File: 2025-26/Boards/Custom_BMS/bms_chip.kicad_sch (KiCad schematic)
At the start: 56 parts, among them J7 Conn_01x06_Pin, J8 15246140, Q1 ZXTN4004KTC, U1 BQ79616PAPRQ1

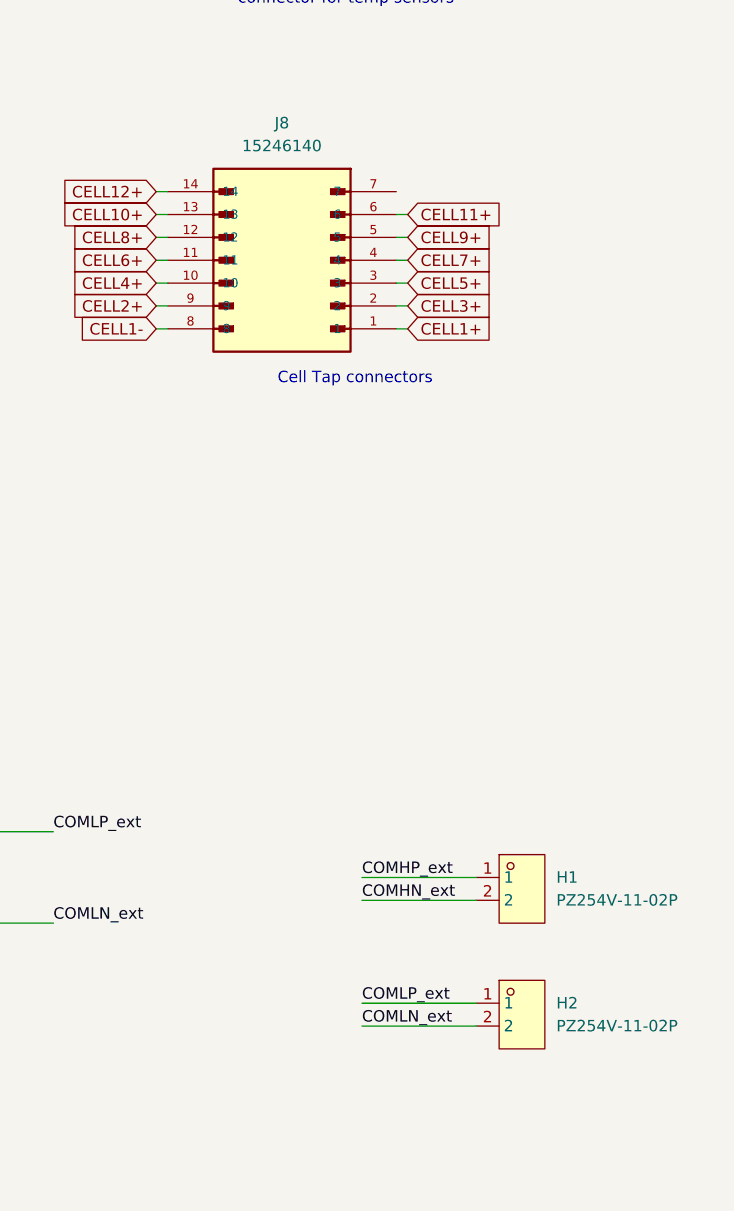
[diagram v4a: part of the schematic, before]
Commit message: fixed some connectors
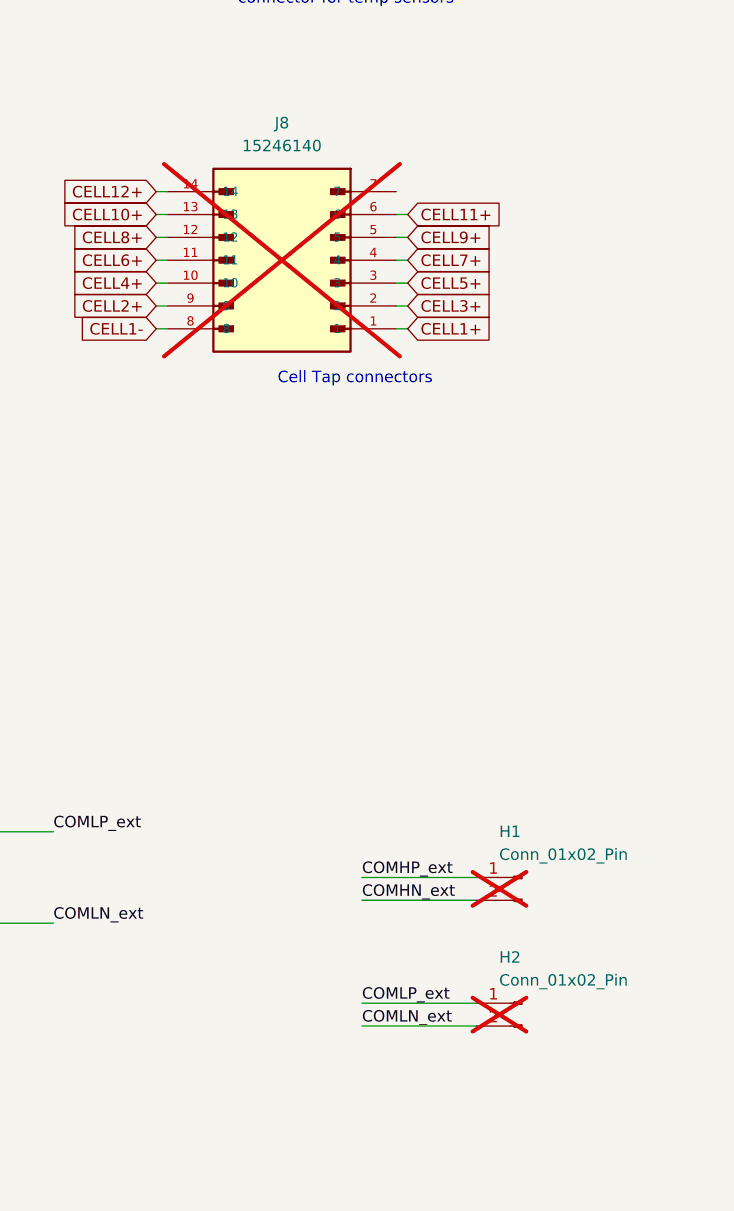
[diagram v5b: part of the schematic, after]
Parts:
- removed H1, H2: PZ254V-11-02P, easyeda2kicad:HDR-TH_2P-P2.54-V-M, symbol easyeda2kicad:PZ254V-11-02P
- added H1, H2: Conn_01x02_Pin, Connector_PinHeader_2.00mm:PinHeader_1x02_P2.00mm_Vertical, symbol Connector:Conn_01x02_Pin
- J8: now not fitted; now left out of the parts list
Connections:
- net COMHN_ext: now also H1.2 (Pin_2)
- net COMHP_ext: now also H1.1 (Pin_1)
- net COMLN_ext: now also H2.2 (Pin_2)
- net COMLP_ext: now also H2.1 (Pin_1)
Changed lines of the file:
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@@
 	)
 	(symbol
+		(lib_id "Connector:Conn_01x02_Pin")
+		(at 377.19 224.79 0)
+		(mirror y)
+		(unit 1)
+		(exclude_from_sim no)
+		(in_bom no)
+		(on_board yes)
+		(dnp yes)
+		(property "Reference" "H2"
+			(at 374.65 219.71 0)
+			(effects
+				(font
+					(size 1.27 1.27)
+				)
+				(justify right)
+			)
+		)
+		(property "Value" "Conn_01x02_Pin"
+			(at 374.65 222.25 0)
+			(effects
+				(font
+					(size 1.27 1.27)
+				)
+				(justify right)
+			)
+		)
+		(property "Footprint" "Connector_PinHeader_2.00mm:PinHeader_1x02_P2.00mm_Vertical"
+			(at 377.19 224.79 0)
+			(effects
+				(font
+					(size 1.27 1.27)
+				)
+				(hide yes)
+			)
+		)
+		(property "Datasheet" "~"
+			(at 377.19 224.79 0)
+			(effects
+				(font
+					(size 1.27 1.27)
+				)
+				(hide yes)
+			)
+		)
+		(property "Description" "Generic connector, single row, 01x02, script generated"
+			(at 377.19 224.79 0)
+			(effects
+				(font
+					(size 1.27 1.27)
+				)
+				(hide yes)
+			)
+		)
+		(pin "1"
+		)
+		(pin "2"
+		)
+		(instances
+			(project "Custom_BMS"
+				(path "/570d6d9c-ebf5-4f83-96f6-d3309a3e637d/730c9124-1e05-4e73-95cf-1be5bb1149a5"
+					(reference "H2")
+					(unit 1)
+				)
+			)
+		)
+	)
+	(symbol
 		(lib_id "PCM_JLCPCB-Resistors:0603,10kΩ")
 		(at 295.91 95.25 90)
@@
 	)
 	(symbol
+		(lib_id "Connector:Conn_01x02_Pin")
+		(at 377.19 210.82 0)
+		(mirror y)
+		(unit 1)
+		(exclude_from_sim no)
+		(in_bom no)
+		(on_board yes)
+		(dnp yes)
+		(property "Reference" "H1"
+			(at 374.65 205.74 0)
+			(effects
+				(font
+					(size 1.27 1.27)
+				)
+				(justify right)
+			)
+		)
+		(property "Value" "Conn_01x02_Pin"
+			(at 374.65 208.28 0)
+			(effects
+				(font
+					(size 1.27 1.27)
+				)
+				(justify right)
+			)
+		)
+		(property "Footprint" "Connector_PinHeader_2.00mm:PinHeader_1x02_P2.00mm_Vertical"
+			(at 377.19 210.82 0)
+			(effects
+				(font
+					(size 1.27 1.27)
+				)
+				(hide yes)
+			)
+		)
+		(property "Datasheet" "~"
+			(at 377.19 210.82 0)
+			(effects
+				(font
+					(size 1.27 1.27)
+				)
+				(hide yes)
+			)
+		)
+		(property "Description" "Generic connector, single row, 01x02, script generated"
+			(at 377.19 210.82 0)
+			(effects
+				(font
+					(size 1.27 1.27)
+				)
+				(hide yes)
+			)
+		)
+		(pin "1"
+		)
+		(pin "2"
+		)
+		(instances
+			(project "Custom_BMS"
+				(path "/570d6d9c-ebf5-4f83-96f6-d3309a3e637d/730c9124-1e05-4e73-95cf-1be5bb1149a5"
+					(reference "H1")
+					(unit 1)
+				)
+			)
+		)
+	)
+	(symbol
 		(lib_id "BQ79616PAPRQ1:BQ79616PAPRQ1")
 		(at 242.57 95.25 0)
@@
 	)
 	(symbol
-		(lib_id "easyeda2kicad:PZ254V-11-02P")
-		(at 377.19 226.06 0)
-		(unit 1)
-		(exclude_from_sim no)
-		(in_bom yes)
-		(on_board yes)
-		(dnp no)
-		(fields_autoplaced yes)
-		(property "Reference" "H2"
-			(at 381 224.7899 0)
-			(effects
-				(font
-					(size 1.27 1.27)
-				)
-				(justify left)
-			)
-		)
-		(property "Value" "PZ254V-11-02P"
-			(at 381 227.3299 0)
-			(effects
-				(font
-					(size 1.27 1.27)
-				)
-				(justify left)
-			)
-		)
-		(property "Footprint" "easyeda2kicad:HDR-TH_2P-P2.54-V-M"
-			(at 377.19 234.95 0)
-			(effects
-				(font
-					(size 1.27 1.27)
-				)
-				(hide yes)
-			)
-		)
-		(property "Datasheet" "https://lcsc.com/product-detail/New-Arrivals_XFCN-PZ254V-11-02P_C492401.html"
-			(at 377.19 237.49 0)
-			(effects
-				(font
-					(size 1.27 1.27)
-				)
-				(hide yes)
-			)
-		)
-		(property "Description" ""
-			(at 377.19 226.06 0)
-			(effects
-				(font
-					(size 1.27 1.27)
-				)
-				(hide yes)
-			)
-		)
-		(property "LCSC Part" "C492401"
-			(at 377.19 240.03 0)
-			(effects
-				(font
-					(size 1.27 1.27)
-				)
-				(hide yes)
-			)
-		)
-		(pin "1"
-		)
-		(pin "2"
-		)
-		(instances
-			(project "Custom_BMS"
-				(path "/570d6d9c-ebf5-4f83-96f6-d3309a3e637d/730c9124-1e05-4e73-95cf-1be5bb1149a5"
-					(reference "H2")
-					(unit 1)
-				)
-			)
-		)
-	)
-	(symbol
 		(lib_id "easyeda2kicad:SM91502ALE")
 		(at 289.56 210.82 0)
@@
 		(unit 1)
 		(exclude_from_sim no)
-		(in_bom yes)
+		(in_bom no)
 		(on_board yes)
-		(dnp no)
+		(dnp yes)
 		(fields_autoplaced yes)
 		(property "Reference" "J8"
@@
 					(unit 1)
 				)
-			)
-		)
-	)
-	(symbol
-		(lib_id "easyeda2kicad:PZ254V-11-02P")
-		(at 377.19 212.09 0)
-		(unit 1)
-		(exclude_from_sim no)
-		(in_bom yes)
-		(on_board yes)
-		(dnp no)
-		(fields_autoplaced yes)
-		(property "Reference" "H1"
-			(at 381 210.8199 0)
-			(effects
-				(font
-					(size 1.27 1.27)
-				)
-				(justify left)
-			)
-		)
-		(property "Value" "PZ254V-11-02P"
-			(at 381 213.3599 0)
-			(effects
-				(font
-					(size 1.27 1.27)
-				)
-				(justify left)
-			)
-		)
-		(property "Footprint" "easyeda2kicad:HDR-TH_2P-P2.54-V-M"
-			(at 377.19 220.98 0)
-			(effects
-				(font
-					(size 1.27 1.27)
-				)
-				(hide yes)
-			)
-		)
-		(property "Datasheet" "https://lcsc.com/product-detail/New-Arrivals_XFCN-PZ254V-11-02P_C492401.html"
-			(at 377.19 223.52 0)
-			(effects
-				(font
-					(size 1.27 1.27)
-				)
-				(hide yes)
-			)
-		)
-		(property "Description" ""
-			(at 377.19 212.09 0)
-			(effects
-				(font
-					(size 1.27 1.27)
-				)
-				(hide yes)
-			)
-		)
-		(property "LCSC Part" "C492401"
-			(at 377.19 226.06 0)
-			(effects
-				(font
-					(size 1.27 1.27)
-				)
-				(hide yes)
-			)
-		)
-		(pin "1"
-		)
-		(pin "2"
-		)
-		(instances
-			(project "Custom_BMS"
-				(path "/570d6d9c-ebf5-4f83-96f6-d3309a3e637d/730c9124-1e05-4e73-95cf-1be5bb1149a5"
-					(reference "H1")
-					(unit 1)
-				)

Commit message: final fixes ??
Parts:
- removed H1, H2: Conn_01x02_Pin, Connector_PinHeader_2.00mm:PinHeader_1x02_P2.00mm_Vertical, symbol Connector:Conn_01x02_Pin
- removed J8: 15246140, easyeda2kicad:MOLEX_15246140, symbol 15246140:15246140
- removed NT1: NetTie_2, NetTie:NetTie-2_SMD_Pad0.5mm, symbol Device:NetTie_2
- removed R41, R42, R43, R44: 10kΩ, PCM_JLCPCB:R_0603, symbol PCM_JLCPCB-Resistors:0603,10kΩ
- removed R77: 100Ω, PCM_JLCPCB:R_0805, symbol PCM_JLCPCB-Resistors:0805,100Ω
- removed R78, R79: AC1210FR-07590RL, easyeda2kicad:R1210, symbol easyeda2kicad:AC1210FR-07590RL
- removed TP2: TestPoint_Small, TestPoint:TestPoint_Pad_D1.0mm, symbol Connector:TestPoint_Small
- added CN1: C4201WR-F-2X8P_C5355564, easyeda2kicad:CONN-TH_C4201WR-F-2X8P, symbol easyeda2kicad:C4201WR-F-2X8P_C5355564
- added CN2, CN3: A2505WV-2P_C5362466, easyeda2kicad:CONN-TH_A2505WV-2P, symbol easyeda2kicad:A2505WV-2P_C5362466
- added R41, R42, R43, R44: 680Ω, PCM_JLCPCB:R_0402, symbol PCM_JLCPCB-Resistors:0402,680Ω
- added R77: CMP2512-FX-1001ELF, Resistor_SMD:R_2512_6332Metric_Pad1.40x3.35mm_HandSolder, symbol Device:R
- added R80: 33Ω, PCM_JLCPCB:R_0402, symbol PCM_JLCPCB-Resistors:0402,33Ω
- C47, C51, C52, D1, L2: now fitted; now in the parts list
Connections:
- net CB_TOP is gone; now on net CB16: C24.2
- net BAT: now also C25.2, R80.1
- net CELL1+: now also CN1.1
- net CELL1-: now also CN1.9
- net CELL10+: now also CN1.14
- net CELL11+: now also CN1.6
- net CELL12+: now also CN1.15
- net CELL2+: now also CN1.10
- net CELL3+: now also CN1.2
- net CELL4+: now also CN1.11
- net CELL5+: now also CN1.3
- net CELL6+: now also CN1.12
- net CELL7+: now also CN1.4
- net CELL8+: now also CN1.13
- net CELL9+: now also CN1.5
- net CELL_TOP: now also R1.2, CN1.16, R77.2, R80.2; no longer C25.2
- net COMHN_ext: now also D1.4, L1.4, CN2.2; no longer D1.6, L1.3
- net COMHP_ext: now also D1.6, L1.3, CN2.1; no longer D1.4, L1.4
- net COMLN_ext: now also CN3.2
- net COMLP_ext: now also CN3.1
- net GND: now also CN1.7
- net TSREF: now also R41.2, R42.2, R43.2, R44.2
- net temp1: now also R41.1
- net temp2: now also R42.1
- net temp3: now also R43.1
- net temp4: now also R44.1
- net at JP4.1 (A): now also R77.1
- net at C45.1, D3.1, R36.2: now also D1.1; no longer D1.3
- net at C45.2: now also L1.2; no longer L1.1
- net VC16: now reaches U1.3 (VC16)
- net VC15: now reaches U1.5 (VC15)
- net VC14: now reaches U1.7 (VC14)
- net VC13: now reaches U1.9 (VC13)
- net at C46.1, D3.2, R37.2: now also D1.3; no longer D1.1
- net at C46.2: now also L1.1; no longer L1.2
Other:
- note added: "upper bound: Rnpn = ((Min VModule) - (VCollector)) / (Max peak current) lower bound: depends on target power dissipation select 2 different Rpn resistors for 4 cells vs 12 cells 4 cells: upper bound = (2.5*4 - 8) / 20mA = 100 Ohms at max V (4.2*4), with 100 ohm resistor, burns 40mW, BJT will burn max 300 mW 12 cells: upper bound = (2.5*12 - 8) / 20mA = 1.1 kOhms at max V (4.2*12), with 1.1 kOhm r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"
- note removed: "upper bound: Rnpn = ((Min VModule) - (VCollector)) / (Max peak current) lower bound: depends on target power dissipation select 2 different Rpn resistors for 4 cells vs 12 cells 4 cells: upper bound = (2.5*4 - 6) / 20mA = 200 Ohms with 200 ohm resistor, burns 80mW, BJT will burn max 136 mW 12 cells: upper bound = (2.5*12 - 6) / 20mA = 1.2 kOhms with 1.2 kOhm resistor, burns 480mW, BJT will burn m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"
- moved on the sheet: C1, C2, C24, C25, C4, C5, C6, C7, C77, C78, TP1, TP25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

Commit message: (2nd) final changes ??
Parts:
- removed CN2, CN3: A2505WV-2P_C5362466, easyeda2kicad:CONN-TH_A2505WV-2P, symbol easyeda2kicad:A2505WV-2P_C5362466
- removed J7: Conn_01x06_Pin, Connector_PinHeader_2.54mm:PinHeader_1x06_P2.54mm_Vertical, symbol Connector:Conn_01x06_Pin
- added CN2, CN3: 0530470210, easyeda2kicad:CONN-TH_0530470210, symbol easyeda2kicad:0530470210
- added CN7: 530470610, easyeda2kicad:CONN-TH_6P-P1.25_530470610, symbol easyeda2kicad:530470610
- CN1: now not fitted; now left out of the parts list
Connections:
- net COMHN_ext: now also CN2.2
- net COMHP_ext: now also CN2.1
- net COMLN_ext: now also CN3.2
- net COMLP_ext: now also CN3.1
- net GND: now also CN7.6
- net TSREF: now also CN7.1
- net temp1: now also CN7.2
- net temp2: now also CN7.3
- net temp3: now also CN7.4
- net temp4: now also CN7.5

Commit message: more gnding changes
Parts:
- removed R35, R38: 1kΩ, PCM_JLCPCB:R_0603, symbol PCM_JLCPCB-Resistors:0603,1kΩ
- added R35, R38: 1kΩ, PCM_JLCPCB:R_0402, symbol PCM_JLCPCB-Resistors:0402,1kΩ
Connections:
- net COMHN: now also R35.2
- net COMHP: now also R35.1
- net COMLN: now also R38.2
- net COMLP: now also R38.1
